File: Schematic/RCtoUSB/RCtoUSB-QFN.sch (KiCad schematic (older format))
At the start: 18 parts, among them J4 USB_B_Mini, J5 SAT, J6 ICSP, Q2 2N7002P_215, U3 AP2210N-3.3TRG1, U4 pic18lf27j53-i_ml

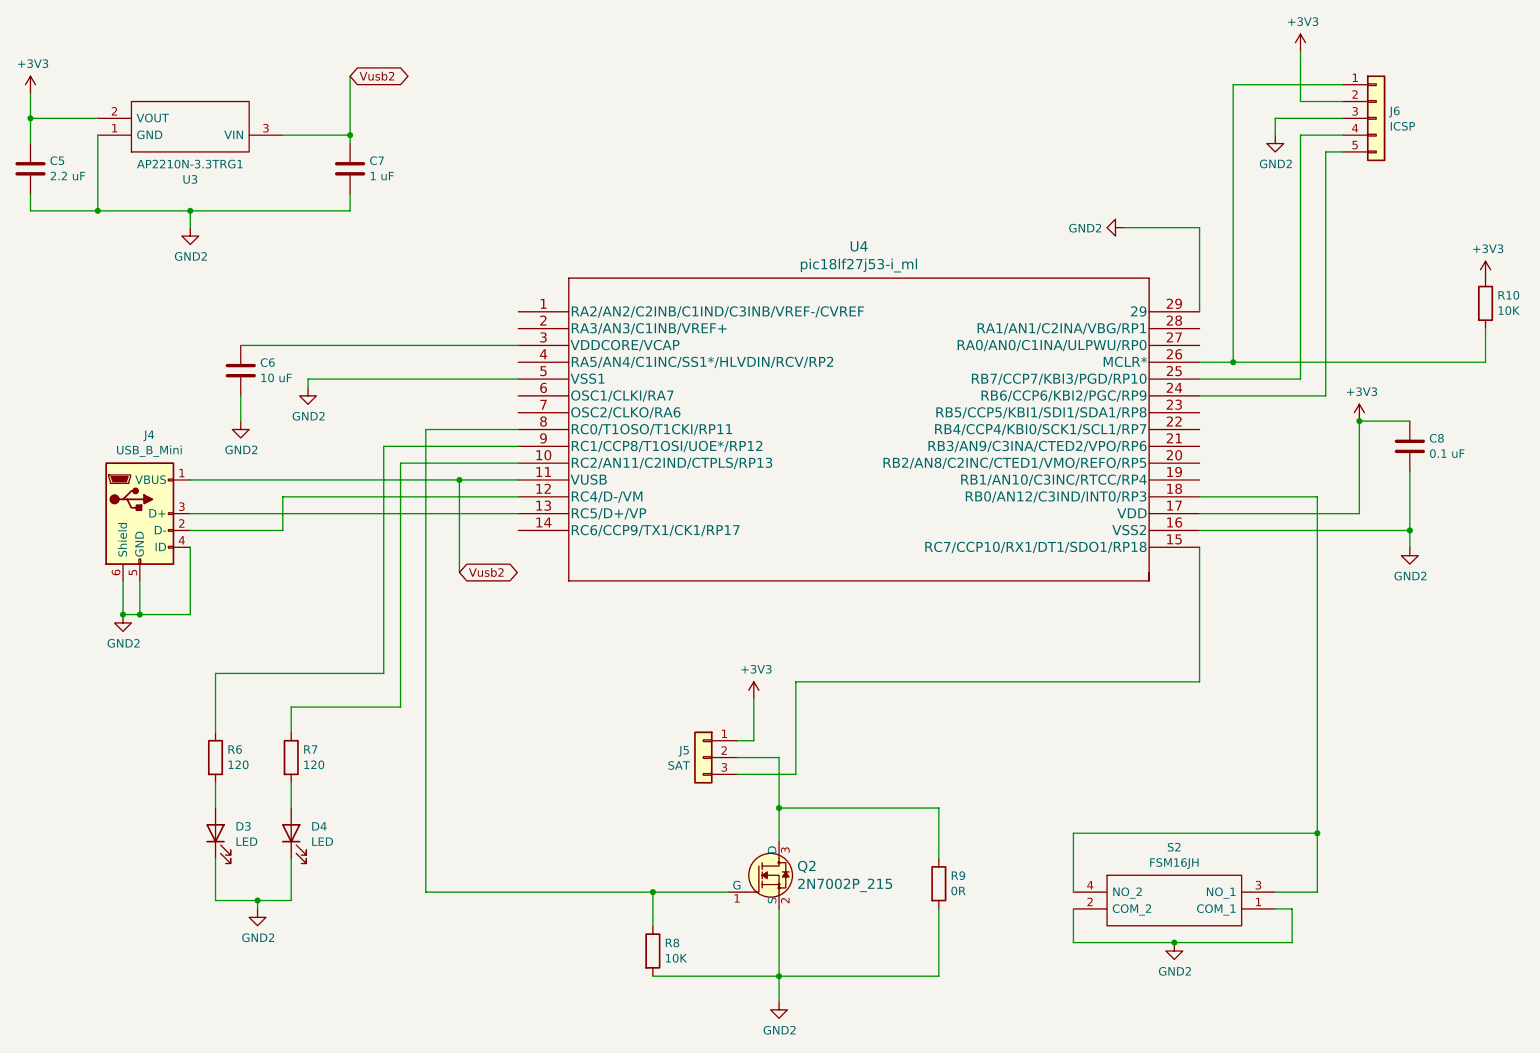
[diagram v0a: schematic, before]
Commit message: Added some breakout connectors to SOIC version
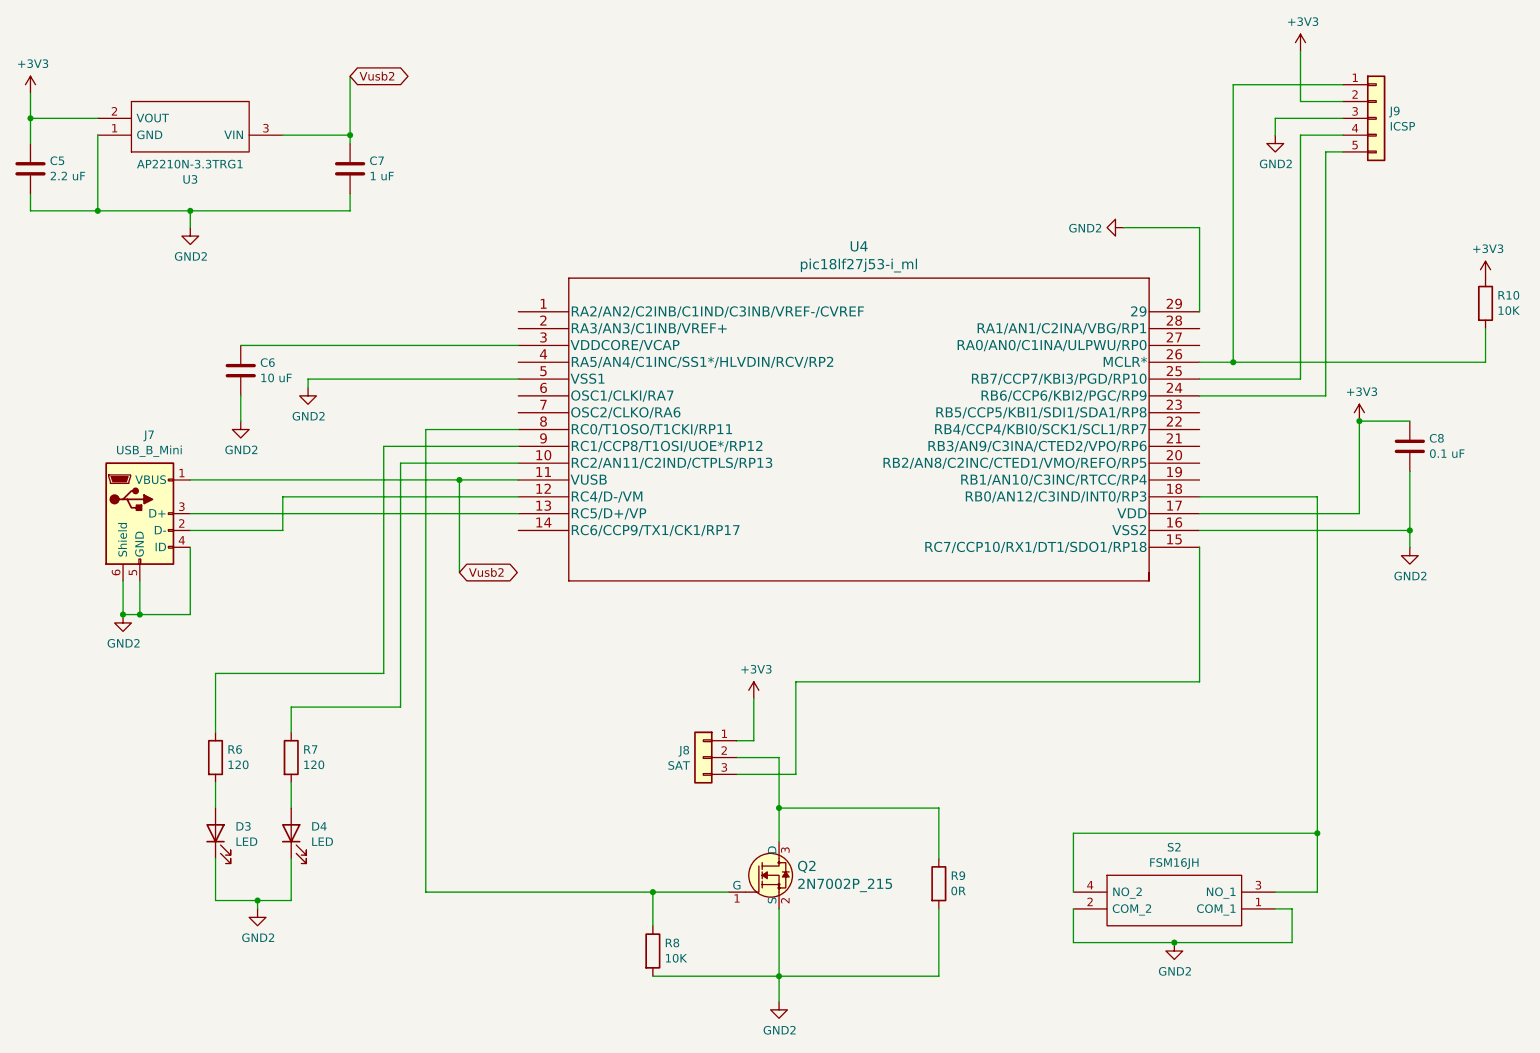
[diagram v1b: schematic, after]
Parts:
- renumbered J4 to J7, J5 to J8, J6 to J9
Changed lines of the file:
@@
 P 9000 1250
 AR Path="/6103280D" Ref="J?"  Part="1"
-AR Path="/60FF3F14/6103280D" Ref="J6"  Part="1"
-F 0 "J6" H 9080 1292 50  0000 L CNN
+AR Path="/60FF3F14/6103280D" Ref="J9"  Part="1"
+F 0 "J9" H 9080 1292 50  0000 L CNN
 F 1 "ICSP" H 9080 1201 50  0000 L CNN
 F 2 "Connector_PinHeader_2.54mm:PinHeader_1x05_P2.54mm_Vertical" H 9000 1250 50  0001 C CNN
@@
 P 5000 5050
 AR Path="/61032813" Ref="J?"  Part="1"
-AR Path="/60FF3F14/61032813" Ref="J5"  Part="1"
-F 0 "J5" H 5080 5092 50  0000 L CNN
+AR Path="/60FF3F14/61032813" Ref="J8"  Part="1"
+F 0 "J8" H 5080 5092 50  0000 L CNN
 F 1 "SAT" H 5080 5001 50  0000 L CNN
 F 2 "JST-withZH:JST_ZH_B3B-ZR_1x03_P1.50mm_Vertical" H 5000 5050 50  0001 C CNN
@@
 P 1650 3600
 AR Path="/61032879" Ref="J?"  Part="1"
-AR Path="/60FF3F14/61032879" Ref="J4"  Part="1"
-F 0 "J4" H 1707 4067 50  0000 C CNN
+AR Path="/60FF3F14/61032879" Ref="J7"  Part="1"
+F 0 "J7" H 1707 4067 50  0000 C CNN
 F 1 "USB_B_Mini" H 1707 3976 50  0000 C CNN
 F 2 "Connector_USB:USB_Mini-B_Wuerth_65100516121_Horizontal" H 1800 3550 50  0001 C CNN
@@
 	7200 6150 7800 6150
 $Comp
-L power:GND2 #PWR017
+L power:GND2 #PWR019
 U 1 1 6103B76F
 P 1950 1900
-F 0 "#PWR017" H 1950 1650 50  0001 C CNN
+F 0 "#PWR019" H 1950 1650 50  0001 C CNN
 F 1 "GND2" H 1955 1727 50  0000 C CNN
 F 2 "" H 1950 1900 50  0001 C CNN
@@
 $EndComp
 $Comp
-L power:GND2 #PWR018
+L power:GND2 #PWR020
 U 1 1 6103BF00
 P 2250 3050
-F 0 "#PWR018" H 2250 2800 50  0001 C CNN
+F 0 "#PWR020" H 2250 2800 50  0001 C CNN
 F 1 "GND2" H 2255 2877 50  0000 C CNN
 F 2 "" H 2250 3050 50  0001 C CNN
@@
 $EndComp
 $Comp
-L power:GND2 #PWR020
+L power:GND2 #PWR022
 U 1 1 6103CABD
 P 2650 2850
-F 0 "#PWR020" H 2650 2600 50  0001 C CNN
+F 0 "#PWR022" H 2650 2600 50  0001 C CNN
 F 1 "GND2" H 2655 2677 50  0000 C CNN
 F 2 "" H 2650 2850 50  0001 C CNN
@@
 $EndComp
 $Comp
-L power:GND2 #PWR019
+L power:GND2 #PWR021
 U 1 1 6103F8C2
 P 2350 5950
-F 0 "#PWR019" H 2350 5700 50  0001 C CNN
+F 0 "#PWR021" H 2350 5700 50  0001 C CNN
 F 1 "GND2" H 2355 5777 50  0000 C CNN
 F 2 "" H 2350 5950 50  0001 C CNN
@@
 $EndComp
 $Comp
-L power:GND2 #PWR022
+L power:GND2 #PWR024
 U 1 1 61042607
 P 5450 6500
-F 0 "#PWR022" H 5450 6250 50  0001 C CNN
+F 0 "#PWR024" H 5450 6250 50  0001 C CNN
 F 1 "GND2" H 5455 6327 50  0000 C CNN
 F 2 "" H 5450 6500 50  0001 C CNN
@@
 $EndComp
 $Comp
-L power:GND2 #PWR024
+L power:GND2 #PWR026
 U 1 1 61045168
 P 7800 6150
-F 0 "#PWR024" H 7800 5900 50  0001 C CNN
+F 0 "#PWR026" H 7800 5900 50  0001 C CNN
 F 1 "GND2" H 7805 5977 50  0000 C CNN
 F 2 "" H 7800 6150 50  0001 C CNN
@@
 $EndComp
 $Comp
-L power:GND2 #PWR016
+L power:GND2 #PWR018
 U 1 1 61047DC4
 P 1550 4200
-F 0 "#PWR016" H 1550 3950 50  0001 C CNN
+F 0 "#PWR018" H 1550 3950 50  0001 C CNN
 F 1 "GND2" H 1555 4027 50  0000 C CNN
 F 2 "" H 1550 4200 50  0001 C CNN
@@
 $EndComp
 $Comp
-L power:GND2 #PWR028
+L power:GND2 #PWR030
 U 1 1 6104A9AD
 P 9200 3800
-F 0 "#PWR028" H 9200 3550 50  0001 C CNN
+F 0 "#PWR030" H 9200 3550 50  0001 C CNN
 F 1 "GND2" H 9205 3627 50  0000 C CNN
 F 2 "" H 9200 3800 50  0001 C CNN
@@
 $EndComp
 $Comp
-L power:GND2 #PWR025
+L power:GND2 #PWR027
 U 1 1 6104D52B
 P 8400 1350
-F 0 "#PWR025" H 8400 1100 50  0001 C CNN
+F 0 "#PWR027" H 8400 1100 50  0001 C CNN
 F 1 "GND2" H 8405 1177 50  0000 C CNN
 F 2 "" H 8400 1350 50  0001 C CNN
@@
 	7800 6150 8500 6150
 $Comp
-L power:+3V3 #PWR026
+L power:+3V3 #PWR028
 U 1 1 61051B9C
 P 8550 850
-F 0 "#PWR026" H 8550 700 50  0001 C CNN
+F 0 "#PWR028" H 8550 700 50  0001 C CNN
 F 1 "+3V3" H 8565 1023 50  0000 C CNN
 F 2 "" H 8550 850 50  0001 C CNN
@@
 $EndComp
 $Comp
-L power:+3V3 #PWR021
+L power:+3V3 #PWR023
 U 1 1 61052C70
 P 5300 4700
-F 0 "#PWR021" H 5300 4550 50  0001 C CNN
+F 0 "#PWR023" H 5300 4550 50  0001 C CNN
 F 1 "+3V3" H 5315 4873 50  0000 C CNN
 F 2 "" H 5300 4700 50  0001 C CNN
@@
 $EndComp
 $Comp
-L power:+3V3 #PWR015
+L power:+3V3 #PWR017
 U 1 1 61053682
 P 1000 1100
-F 0 "#PWR015" H 1000 950 50  0001 C CNN
+F 0 "#PWR017" H 1000 950 50  0001 C CNN
 F 1 "+3V3" H 1015 1273 50  0000 C CNN
 F 2 "" H 1000 1100 50  0001 C CNN
@@
 $EndComp
 $Comp
-L power:+3V3 #PWR029
+L power:+3V3 #PWR031
 U 1 1 61054199
 P 9650 2200
-F 0 "#PWR029" H 9650 2050 50  0001 C CNN
+F 0 "#PWR031" H 9650 2050 50  0001 C CNN
 F 1 "+3V3" H 9665 2373 50  0000 C CNN
 F 2 "" H 9650 2200 50  0001 C CNN
@@
 	7950 2700 8150 2700
 $Comp
-L power:+3V3 #PWR027
+L power:+3V3 #PWR029
 U 1 1 61052632
 P 8900 3050
-F 0 "#PWR027" H 8900 2900 50  0001 C CNN
+F 0 "#PWR029" H 8900 2900 50  0001 C CNN
 F 1 "+3V3" H 8915 3223 50  0000 C CNN
 F 2 "" H 8900 3050 50  0001 C CNN
@@
 	5550 4600 7950 4600
 $Comp
-L power:GND2 #PWR023
+L power:GND2 #PWR025
 U 1 1 610C3873
 P 7500 1900
-F 0 "#PWR023" H 7500 1650 50  0001 C CNN
+F 0 "#PWR025" H 7500 1650 50  0001 C CNN
 F 1 "GND2" V 7505 1772 50  0000 R CNN
 F 2 "" H 7500 1900 50  0001 C CNN

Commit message: PCB layout
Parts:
- C5, C6, C7, C8: footprint Capacitor_SMD:C_0805_2012Metric -> Capacitor_SMD:C_0603_1608Metric
- D3, D4: footprint LED_SMD:LED_0805_2012Metric -> LED_SMD:LED_0603_1608Metric
- R10, R6, R7, R8, R9: footprint Resistor_SMD:R_0805_2012Metric -> Resistor_SMD:R_0603_1608Metric
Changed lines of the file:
@@
 F 0 "C5" H 1115 1596 50  0000 L CNN
 F 1 "2.2 uF" H 1115 1505 50  0000 L CNN
-F 2 "Capacitor_SMD:C_0805_2012Metric" H 1038 1400 50  0001 C CNN
+F 2 "Capacitor_SMD:C_0603_1608Metric" H 1038 1400 50  0001 C CNN
 F 3 "~" H 1000 1550 50  0001 C CNN
 	1    1000 1550
@@
 F 0 "C7" H 3015 1596 50  0000 L CNN
 F 1 "1 uF" H 3015 1505 50  0000 L CNN
-F 2 "Capacitor_SMD:C_0805_2012Metric" H 2938 1400 50  0001 C CNN
+F 2 "Capacitor_SMD:C_0603_1608Metric" H 2938 1400 50  0001 C CNN
 F 3 "~" H 2900 1550 50  0001 C CNN
 	1    2900 1550
@@
 F 0 "R6" H 2170 5096 50  0000 L CNN
 F 1 "120" H 2170 5005 50  0000 L CNN
-F 2 "Resistor_SMD:R_0805_2012Metric" V 2030 5050 50  0001 C CNN
+F 2 "Resistor_SMD:R_0603_1608Metric" V 2030 5050 50  0001 C CNN
 F 3 "~" H 2100 5050 50  0001 C CNN
 	1    2100 5050
@@
 F 0 "R7" H 2620 5096 50  0000 L CNN
 F 1 "120" H 2620 5005 50  0000 L CNN
-F 2 "Resistor_SMD:R_0805_2012Metric" V 2480 5050 50  0001 C CNN
+F 2 "Resistor_SMD:R_0603_1608Metric" V 2480 5050 50  0001 C CNN
 F 3 "~" H 2550 5050 50  0001 C CNN
 	1    2550 5050
@@
 F 0 "R10" H 9720 2396 50  0000 L CNN
 F 1 "10K" H 9720 2305 50  0000 L CNN
-F 2 "Resistor_SMD:R_0805_2012Metric" V 9580 2350 50  0001 C CNN
+F 2 "Resistor_SMD:R_0603_1608Metric" V 9580 2350 50  0001 C CNN
 F 3 "~" H 9650 2350 50  0001 C CNN
 	1    9650 2350
@@
 F 0 "C6" H 2365 2796 50  0000 L CNN
 F 1 "10 uF" H 2365 2705 50  0000 L CNN
-F 2 "Capacitor_SMD:C_0805_2012Metric" H 2288 2600 50  0001 C CNN
+F 2 "Capacitor_SMD:C_0603_1608Metric" H 2288 2600 50  0001 C CNN
 F 3 "~" H 2250 2750 50  0001 C CNN
 	1    2250 2750
@@
 F 0 "C8" H 9315 3246 50  0000 L CNN
 F 1 "0.1 uF" H 9315 3155 50  0000 L CNN
-F 2 "Capacitor_SMD:C_0805_2012Metric" H 9238 3050 50  0001 C CNN
+F 2 "Capacitor_SMD:C_0603_1608Metric" H 9238 3050 50  0001 C CNN
 F 3 "~" H 9200 3200 50  0001 C CNN
 	1    9200 3200
@@
 F 0 "R8" H 4770 6246 50  0000 L CNN
 F 1 "10K" H 4770 6155 50  0000 L CNN
-F 2 "Resistor_SMD:R_0805_2012Metric" V 4630 6200 50  0001 C CNN
+F 2 "Resistor_SMD:R_0603_1608Metric" V 4630 6200 50  0001 C CNN
 F 3 "~" H 4700 6200 50  0001 C CNN
 	1    4700 6200
@@
 F 0 "D3" V 2139 5382 50  0000 R CNN
 F 1 "LED" V 2048 5382 50  0000 R CNN
-F 2 "LED_SMD:LED_0805_2012Metric" H 2100 5500 50  0001 C CNN
+F 2 "LED_SMD:LED_0603_1608Metric" H 2100 5500 50  0001 C CNN
 F 3 "~" H 2100 5500 50  0001 C CNN
 	1    2100 5500
@@
 F 0 "D4" V 2589 5382 50  0000 R CNN
 F 1 "LED" V 2498 5382 50  0000 R CNN
-F 2 "LED_SMD:LED_0805_2012Metric" H 2550 5500 50  0001 C CNN
+F 2 "LED_SMD:LED_0603_1608Metric" H 2550 5500 50  0001 C CNN
 F 3 "~" H 2550 5500 50  0001 C CNN
 	1    2550 5500
@@
 F 0 "R9" H 6470 5846 50  0000 L CNN
 F 1 "0R" H 6470 5755 50  0000 L CNN
-F 2 "Resistor_SMD:R_0805_2012Metric" V 6330 5800 50  0001 C CNN
+F 2 "Resistor_SMD:R_0603_1608Metric" V 6330 5800 50  0001 C CNN
 F 3 "~" H 6400 5800 50  0001 C CNN
 	1    6400 5800

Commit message: Finished schematic and pcb
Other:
- note added: "Do not populate R9"
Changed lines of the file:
@@
 Wire Wire Line
 	3550 3400 3900 3400
+Text Notes 6150 6000 0    50   ~ 0
+Do not populate R9
 $EndSCHEMATC

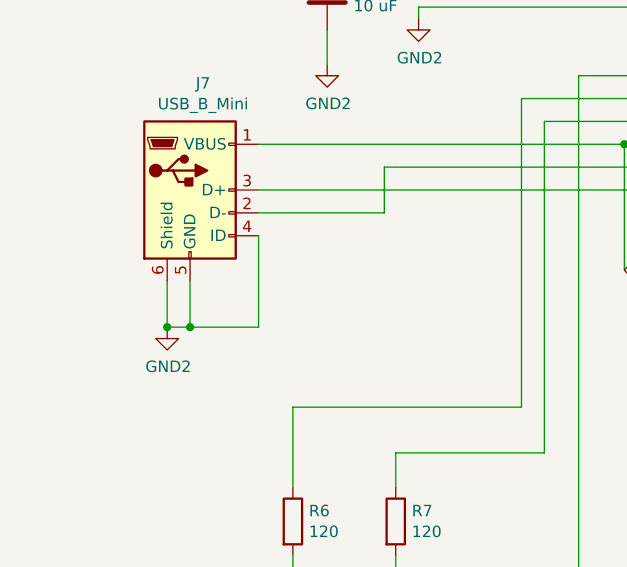
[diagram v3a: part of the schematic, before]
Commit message: Changed ID pin to floating on USB connector
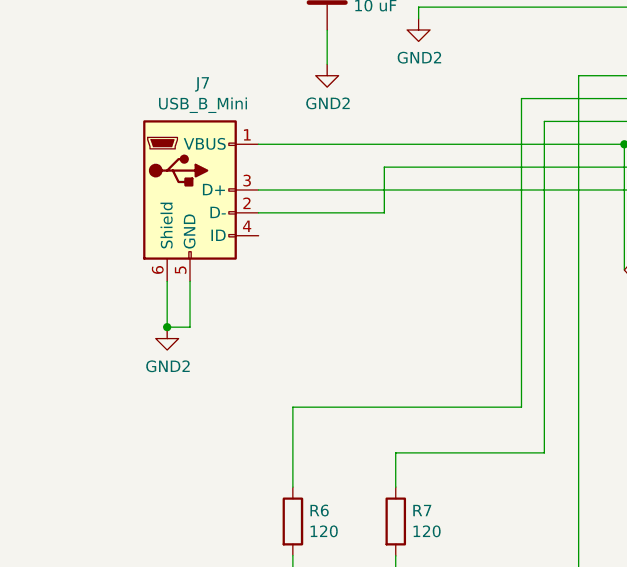
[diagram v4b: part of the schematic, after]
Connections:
- net GND2: no longer J7.4 (ID)
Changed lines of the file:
@@
 	2500 3500 3900 3500
 Wire Wire Line
-	1950 3800 1950 4200
-Wire Wire Line
-	1950 4200 1650 4200
-Wire Wire Line
 	1650 4000 1650 4200
-Connection ~ 1650 4200
 Wire Wire Line
 	1650 4200 1550 4200

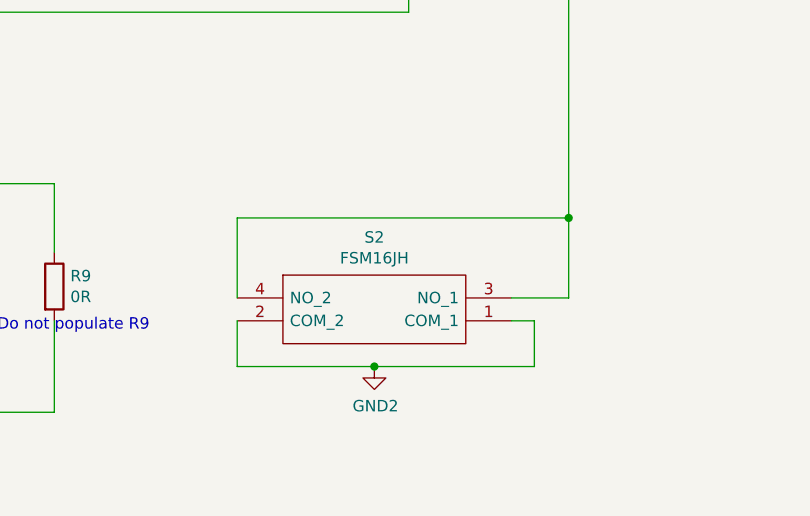
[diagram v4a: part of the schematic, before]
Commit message: Improved switch symbol in schematic
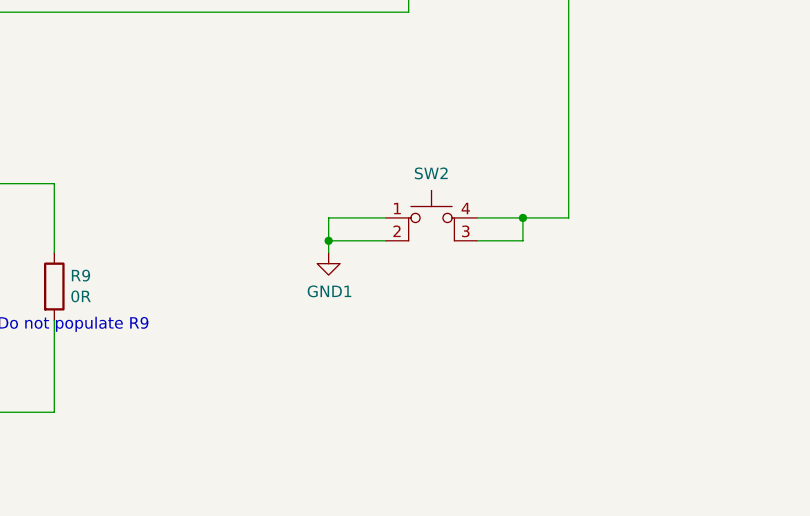
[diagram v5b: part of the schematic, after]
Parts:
- removed S2: FSM16JH, SamacSys_Parts:FSM16JH, symbol SamacSys_Parts:FSM16JH
- added SW2: SW_MEC_5E, SamacSys_Parts:FSM16JH, symbol Switch:SW_MEC_5E
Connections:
- net at U4.18 (RB0/AN12/C3IND/INT0/RP3): now also SW2.3 (K), SW2.4 (A)
- new net GND1: SW2.1, SW2.2
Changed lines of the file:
@@
-$EndComp
-$Comp
-L SamacSys_Parts:FSM16JH S?
-U 1 1 6103288B
-P 7200 5850
-AR Path="/6103288B" Ref="S?"  Part="1"
-AR Path="/60FF3F14/6103288B" Ref="S2"  Part="1"
-F 0 "S2" H 7800 6115 50  0000 C CNN
-F 1 "FSM16JH" H 7800 6024 50  0000 C CNN
-F 2 "SamacSys_Parts:FSM16JH" H 8250 5950 50  0001 L CNN
-F 3 "https://www.te.com/commerce/DocumentDelivery/DDEController?Action=showdoc&DocId=Customer+Drawing%7F1825910%7FC10%7Fpdf%7FEnglish%7FENG_CD_1825910_C10.pdf%7F3-1825910-1" H 8250 5850 50  0001 L CNN
-F 4 "Tactile Switches 6MM TACT SWITCH" H 8250 5750 50  0001 L CNN "Description"
-F 5 "17.3" H 8250 5650 50  0001 L CNN "Height"
-F 6 "506-FSM16JH" H 8250 5550 50  0001 L CNN "Mouser Part Number"
-F 7 "https://www.mouser.co.uk/ProductDetail/TE-Connectivity-PB/FSM16JH/?qs=eA0sQYb2Mifk48vugSh4aw%3D%3D" H 8250 5450 50  0001 L CNN "Mouser Price/Stock"
-F 8 "TE Connectivity" H 8250 5350 50  0001 L CNN "Manufacturer_Name"
-F 9 "FSM16JH" H 8250 5250 50  0001 L CNN "Manufacturer_Part_Number"
-	1    7200 5850
-	1    0    0    -1
 $EndComp
 $Comp
@@
 	8700 1450 8800 1450
 Wire Wire Line
-	8650 5850 8400 5850
-Wire Wire Line
-	8400 5950 8500 5950
-Wire Wire Line
-	8500 5950 8500 6150
-Wire Wire Line
-	7200 5850 7200 5500
-Wire Wire Line
-	7200 5500 8650 5500
-Wire Wire Line
-	8650 5500 8650 5850
-Wire Wire Line
-	7200 5950 7200 6150
-Wire Wire Line
 	3100 4550 2100 4550
 Wire Wire Line
@@
 Text GLabel 2900 1000 2    50   BiDi ~ 0
 Vusb2
-Wire Wire Line
-	7200 6150 7800 6150
 $Comp
 L power:GND2 #PWR019
@@
 $EndComp
 $Comp
-L power:GND2 #PWR026
-U 1 1 61045168
-P 7800 6150
-F 0 "#PWR026" H 7800 5900 50  0001 C CNN
-F 1 "GND2" H 7805 5977 50  0000 C CNN
-F 2 "" H 7800 6150 50  0001 C CNN
-F 3 "" H 7800 6150 50  0001 C CNN
-	1    7800 6150
-	1    0    0    -1
-$EndComp
-$Comp
 L power:GND2 #PWR018
 U 1 1 61047DC4
@@
 	1    0    0    -1
 $EndComp
-Connection ~ 7800 6150
-Wire Wire Line
-	7800 6150 8500 6150
 $Comp
 L power:+3V3 #PWR028
@@
 Wire Wire Line
 	8650 3500 8650 5500
-Connection ~ 8650 5500
 Wire Wire Line
 	7950 3600 8900 3600
@@
 Text Notes 6150 6000 0    50   ~ 0
 Do not populate R9
+$Comp
+L power:GND1 #PWR?
+U 1 1 616D9252
+P 7600 5650
+F 0 "#PWR?" H 7600 5400 50  0001 C CNN
+F 1 "GND1" H 7605 5477 50  0000 C CNN
+F 2 "" H 7600 5650 50  0001 C CNN
+F 3 "" H 7600 5650 50  0001 C CNN
+	1    7600 5650
+	1    0    0    -1
+$EndComp
+$Comp
+L Switch:SW_MEC_5E SW?
+U 1 1 616D9258
+P 8050 5600
+AR Path="/616D9258" Ref="SW?"  Part="1"
+AR Path="/60FF3F14/616D9258" Ref="SW2"  Part="1"
+F 0 "SW2" H 8050 5893 50  0000 C CNN
+F 1 "SW_MEC_5E" H 8050 5894 50  0001 C CNN
+F 2 "SamacSys_Parts:FSM16JH" H 8050 5900 50  0001 C CNN
+F 3 "http://www.apem.com/int/index.php?controller=attachment&id_attachment=1371" H 8050 5900 50  0001 C CNN
+	1    8050 5600
+	1    0    0    -1
+$EndComp
+Wire Wire Line
+	8250 5500 8450 5500
+Wire Wire Line
+	8250 5600 8450 5600
+Wire Wire Line
+	8450 5600 8450 5500
+Connection ~ 8450 5500
+Wire Wire Line
+	8450 5500 8650 5500
+Wire Wire Line
+	7850 5600 7600 5600
+Wire Wire Line
+	7600 5600 7600 5650
+Wire Wire Line
+	7850 5500 7600 5500
+Wire Wire Line
+	7600 5500 7600 5600
+Connection ~ 7600 5600
 $EndSCHEMATC
